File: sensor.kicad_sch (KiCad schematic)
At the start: 35 parts, among them J5 Conn_01x07_Pin, J8 Conn_01x08_Pin, U3 MIC5323-3.3YD5-TR

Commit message: Cleanup libraries
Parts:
- LED6: symbol marbastlib:SK6812MINI-E -> Marbastlib:SK6812MINI-E
- U3: symbol mcp5323:MIC5323-3.3YD5-TR -> Mcp5323:MIC5323-3.3YD5-TR
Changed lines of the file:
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@@
     )
   )
-  (symbol (lib_id "marbastlib:SK6812MINI-E") (at 204.47 91.44 0) (unit 1)
+  (symbol (lib_id "Marbastlib:SK6812MINI-E") (at 204.47 91.44 0) (unit 1)
     (in_bom yes) (on_board yes) (dnp no)
     (property "Reference" "LED6" (at 210.82 99.06 0)
@@
     )
   )
-  (symbol (lib_id "mcp5323:MIC5323-3.3YD5-TR") (at 189.23 34.29 0) (unit 1)
+  (symbol (lib_id "Mcp5323:MIC5323-3.3YD5-TR") (at 189.23 34.29 0) (unit 1)
     (in_bom yes) (on_board yes) (dnp no) (fields_autoplaced)
     (property "Reference" "U3" (at 203.2 26.67 0)

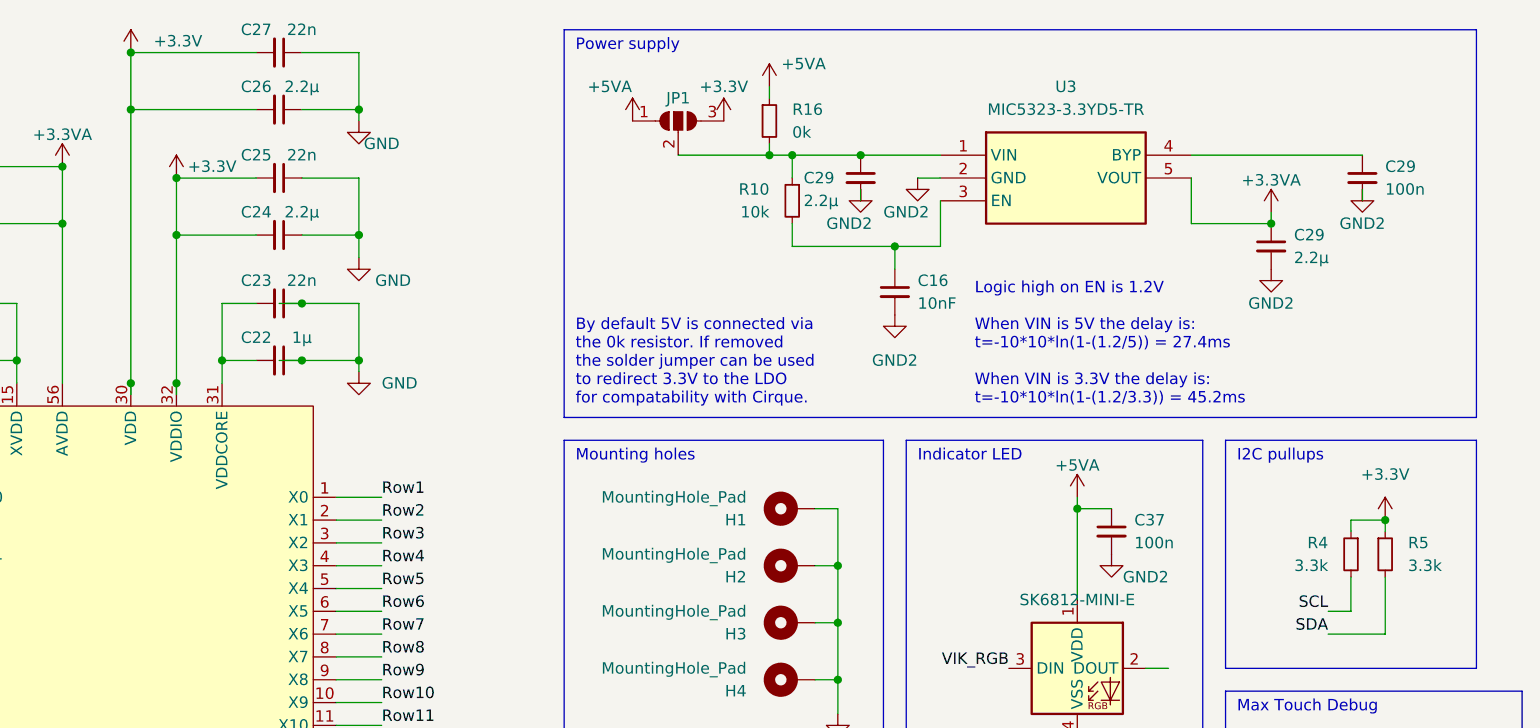
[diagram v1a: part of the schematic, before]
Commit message: Switch LDO for a cheaper part.
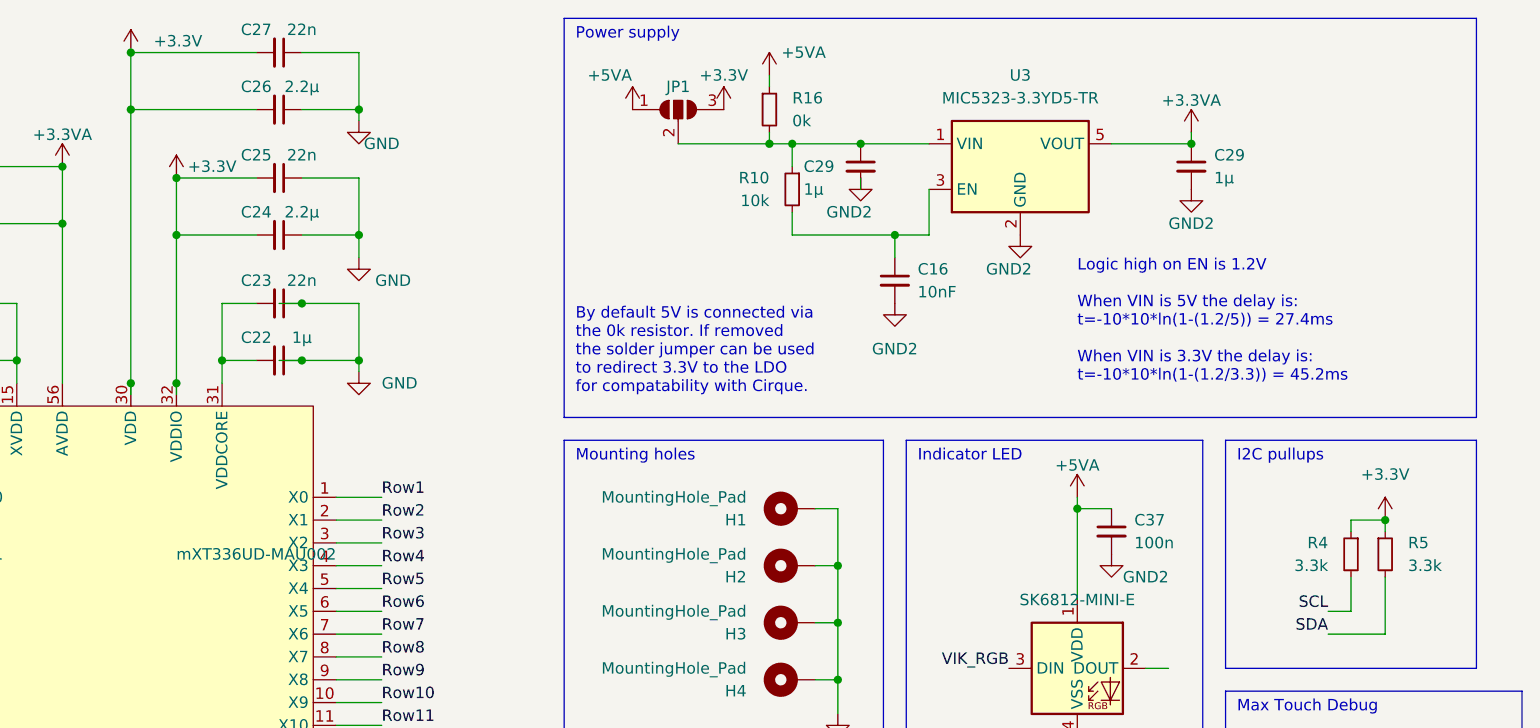
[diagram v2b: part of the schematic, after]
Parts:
- removed C29: 100n, Capacitor_SMD:C_0402_1005Metric, symbol Device:C_Small
- C29: value 2.2µ -> 1µ
- U3: footprint Trackpad:SOT95P280X100-5N -> Package_TO_SOT_SMD:SOT-23-5; symbol Mcp5323:MIC5323-3.3YD5-TR -> Regulator_Linear:MIC5504-3.3YM5; LCSC C512211 -> C88419
- mXT336UD-MAU1: value ~ -> mXT336UD-MAU002
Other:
- moved on the sheet: C16, C29, JP1, R10, R16

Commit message: Move USB port closer to the edge, Additional silkscreen, Add reset header, shrink LDO caps, swap QSPI flash.
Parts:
- C29: footprint Capacitor_SMD:C_0603_1608Metric -> Capacitor_SMD:C_0402_1005Metric
- U3: LCSC C88419 -> C512211
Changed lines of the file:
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@@
       (effects (font (size 1.27 1.27)) (justify left))
     )
-    (property "Footprint" "Capacitor_SMD:C_0603_1608Metric" (at 217.17 35.56 0)
+    (property "Footprint" "Capacitor_SMD:C_0402_1005Metric" (at 217.17 35.56 0)
       (effects (font (size 1.27 1.27)) hide)
     )
@@
       (effects (font (size 1.27 1.27)) (justify left))
     )
-    (property "Footprint" "Capacitor_SMD:C_0603_1608Metric" (at 180.34 35.56 0)
+    (property "Footprint" "Capacitor_SMD:C_0402_1005Metric" (at 180.34 35.56 0)
       (effects (font (size 1.27 1.27)) hide)
     )
@@
       (effects (font (size 1.27 1.27)) (justify left top) hide)
     )
-    (property "LCSC" "C88419" (at 212.09 27.94 0)
-      (effects (font (size 1.27 1.27)) hide)
-    )
+    (property "LCSC" "C512211" (at 212.09 27.94 0)
+      (effects (font (size 1.27 1.27)) hide)
+    )

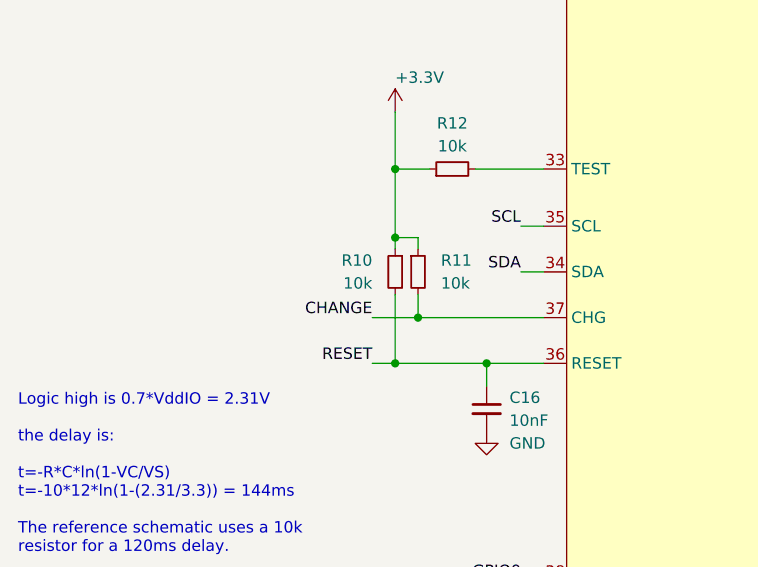
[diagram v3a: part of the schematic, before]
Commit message: Re-route to avoid crossing the USB data lines. Reduced keys to 5 to avoid having to route a long trace around the crystal, swaped key footprint from choc hotswap to mx/choc combined soldered.
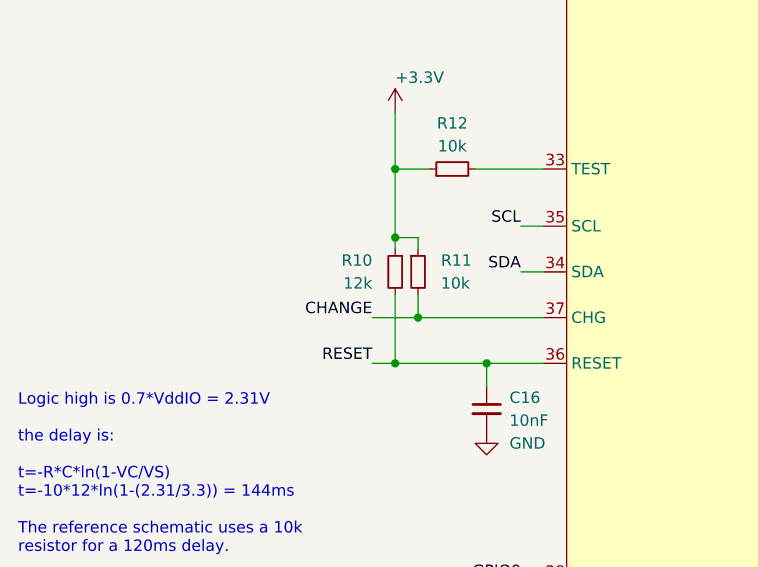
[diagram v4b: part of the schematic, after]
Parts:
- R10: value 10k -> 12k
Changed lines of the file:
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@@
       (effects (font (size 1.27 1.27)) (justify left))
     )
-    (property "Value" "10k" (at 55.88 125.73 0)
+    (property "Value" "12k" (at 55.88 125.73 0)
       (effects (font (size 1.27 1.27)) (justify left))
     )

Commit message: Minor cleanups. Made the mounting hole distances round numbers, cleaned up a few traces.
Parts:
- added J10: Conn_01x01_Pin, Connector_PinHeader_1.27mm:PinHeader_1x01_P1.27mm_Vertical, symbol Connector:Conn_01x01_Pin
- LED6: LCSC C5200774 -> C5149201
- U3: value MIC5323-3.3YD5-TR -> MIC5504-3.3YM5; LCSC C512211 -> C88419
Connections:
- net +3.3VA: now also J10.1 (Pin_1)
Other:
- note added: "AVCC 3.3V"
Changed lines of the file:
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@@
+    (stroke (width 0) (type default))
+  )
+  (wire (pts (xy 238.76 135.89) (xy 246.38 135.89))
     (stroke (width 0) (type default))
   )
@@
   (wire (pts (xy 68.58 134.62) (xy 74.93 134.62))
     (stroke (width 0) (type default))
+  )
+  (rectangle (start 220.98 125.73) (end 254 139.7)
+    (stroke (width 0) (type default))
+    (fill (type none))
   )
   (rectangle (start 147.32 19.05) (end 248.92 63.5)
@@
     (effects (font (size 1.27 1.27)) (justify left bottom))
   )
+  (text "AVCC 3.3V" (at 222.25 128.27 0)
+    (effects (font (size 1.27 1.27)) (justify left bottom))
+  )
   (text "Max Touch Debug" (at 222.25 96.52 0)
     (effects (font (size 1.27 1.27)) (justify left bottom))
@@
         (path "/3796446b-0052-4d89-b512-07a2e9135d0d/2780c9a8-e5e0-42e8-93d7-9eb6f8aa439b"
           (reference "J5") (unit 1)
+        )
+      )
+    )
+  )
+  (symbol (lib_id "Connector:Conn_01x01_Pin") (at 233.68 135.89 0) (unit 1)
+    (in_bom yes) (on_board yes) (dnp no) (fields_autoplaced)
+    (property "Reference" "J10" (at 234.315 130.81 0)
+      (effects (font (size 1.27 1.27)))
+    )
+    (property "Value" "Conn_01x01_Pin" (at 234.315 133.35 0)
+      (effects (font (size 1.27 1.27)))
+    )
+    (property "Footprint" "Connector_PinHeader_1.27mm:PinHeader_1x01_P1.27mm_Vertical" (at 233.68 135.89 0)
+      (effects (font (size 1.27 1.27)) hide)
+    )
+    (property "Datasheet" "~" (at 233.68 135.89 0)
+      (effects (font (size 1.27 1.27)) hide)
+    )
+    (pin "1")
+    (instances
+      (project "trackpad"
+        (path "/3796446b-0052-4d89-b512-07a2e9135d0d/2780c9a8-e5e0-42e8-93d7-9eb6f8aa439b"
+          (reference "J10") (unit 1)
         )
       )
@@
         (path "/3796446b-0052-4d89-b512-07a2e9135d0d/2780c9a8-e5e0-42e8-93d7-9eb6f8aa439b"
           (reference "#PWR079") (unit 1)
+        )
+      )
+    )
+  )
+  (symbol (lib_id "power:+3.3VA") (at 246.38 135.89 0) (unit 1)
+    (in_bom yes) (on_board yes) (dnp no)
+    (property "Reference" "#PWR016" (at 246.38 139.7 0)
+      (effects (font (size 1.27 1.27)) hide)
+    )
+    (property "Value" "+3.3VA" (at 246.38 132.334 0)
+      (effects (font (size 1.27 1.27)))
+    )
+    (property "Footprint" "" (at 246.38 135.89 0)
+      (effects (font (size 1.27 1.27)) hide)
+    )
+    (property "Datasheet" "" (at 246.38 135.89 0)
+      (effects (font (size 1.27 1.27)) hide)
+    )
+    (pin "1")
+    (instances
+      (project "trackpad"
+        (path "/3796446b-0052-4d89-b512-07a2e9135d0d"
+          (reference "#PWR016") (unit 1)
+        )
+        (path "/3796446b-0052-4d89-b512-07a2e9135d0d/efc97fde-28db-4fd6-89b1-84dafa779b4e"
+          (reference "#PWR048") (unit 1)
+        )
+        (path "/3796446b-0052-4d89-b512-07a2e9135d0d/2780c9a8-e5e0-42e8-93d7-9eb6f8aa439b"
+          (reference "#PWR066") (unit 1)
         )
       )
@@
       (effects (font (size 1.27 1.27)) hide)
     )
-    (property "LCSC" "C5200774" (at 210.82 99.06 0)
+    (property "LCSC" "C5149201" (at 210.82 99.06 0)
       (effects (font (size 1.27 1.27)) hide)
     )
@@
         )
         (path "/3796446b-0052-4d89-b512-07a2e9135d0d/2780c9a8-e5e0-42e8-93d7-9eb6f8aa439b"
-          (reference "LED7") (unit 1)
+          (reference "LED6") (unit 1)
         )
       )
@@
       (effects (font (size 1.27 1.27)))
     )
-    (property "Value" "MIC5323-3.3YD5-TR" (at 198.12 27.94 0)
+    (property "Value" "MIC5504-3.3YM5" (at 198.12 27.94 0)
       (effects (font (size 1.27 1.27)))
     )
@@
       (effects (font (size 1.27 1.27)) (justify left top) hide)
     )
-    (property "LCSC" "C512211" (at 212.09 27.94 0)
-      (effects (font (size 1.27 1.27)) hide)
-    )
+    (property "LCSC" "C88419" (at 212.09 27.94 0)
+      (effects (font (size 1.27 1.27)) hide)
+    )

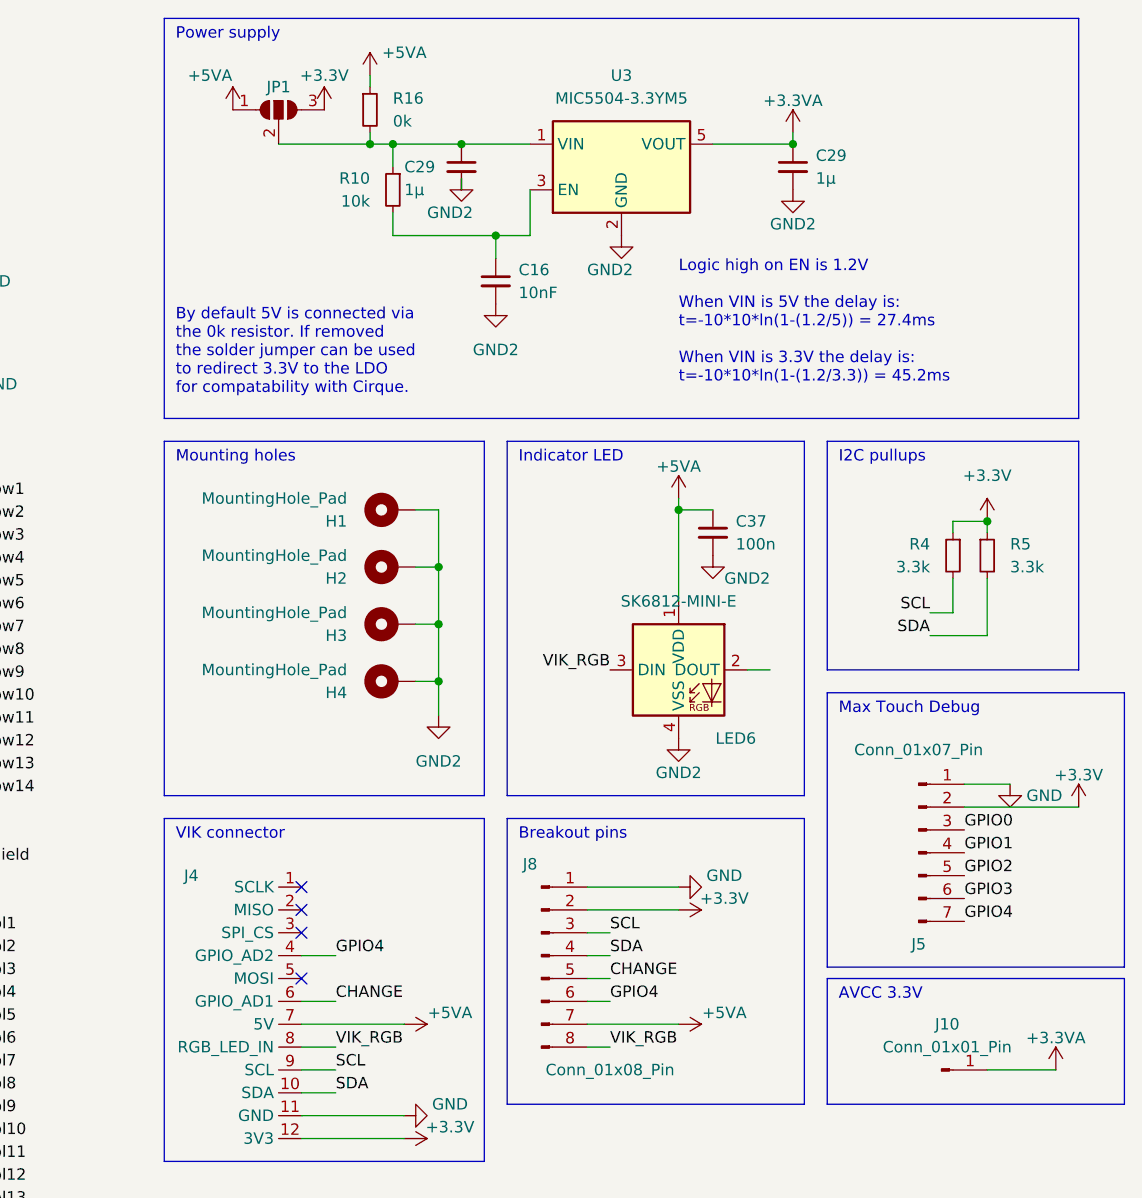
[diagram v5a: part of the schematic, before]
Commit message: Modify EC11 footprint to allow SMT parts. Add resistors to the LED data lines.
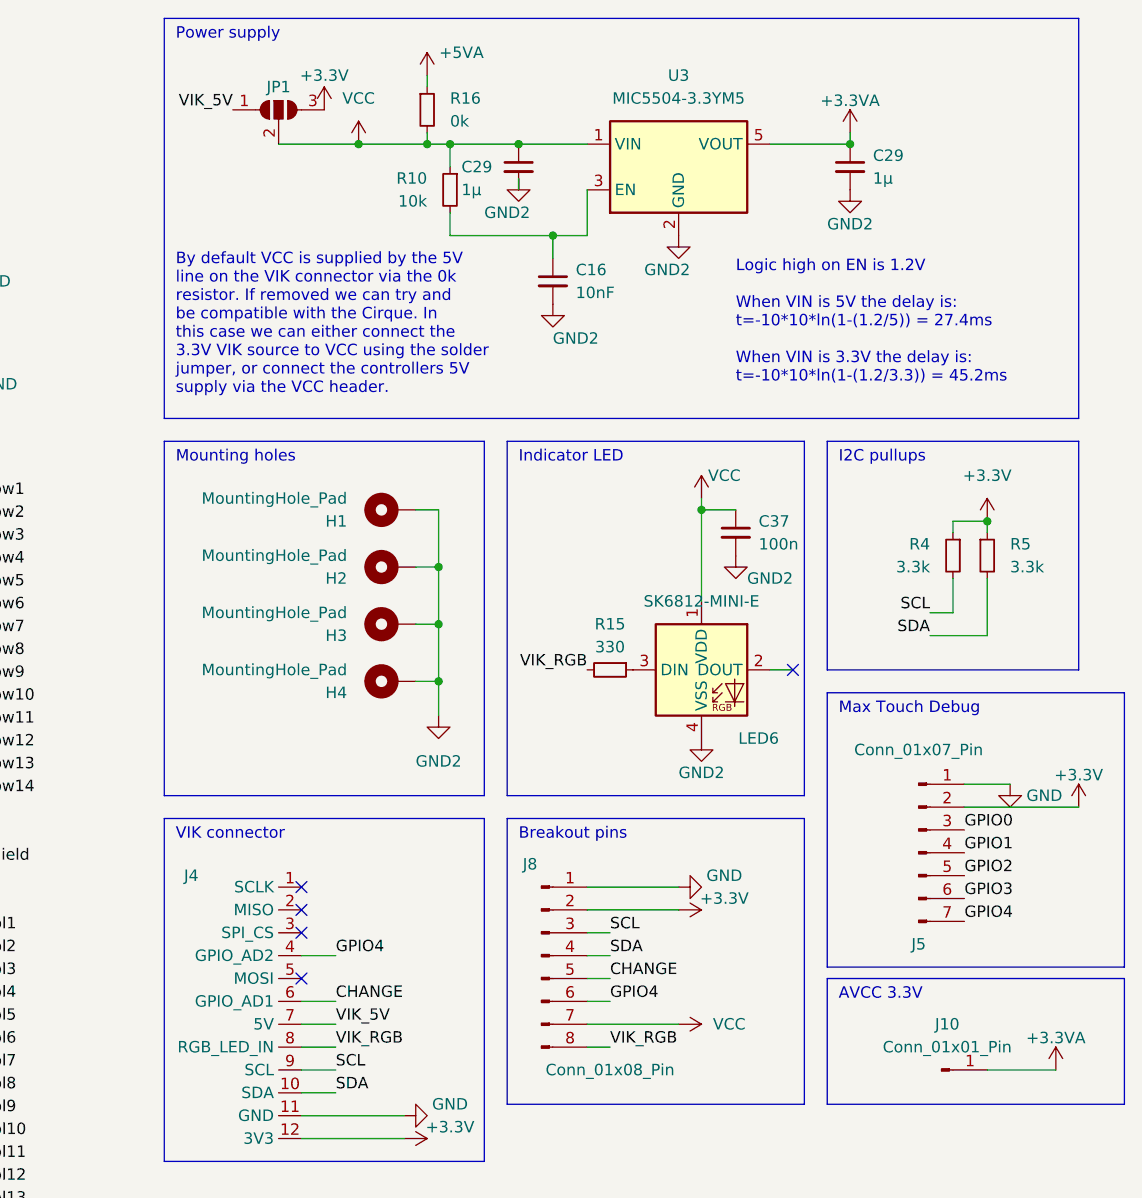
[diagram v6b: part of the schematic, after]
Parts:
- added R15: 330, Resistor_SMD:R_0402_1005Metric, symbol Device:R_Small
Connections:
- net +5VA: no longer C37.1, J4.7 (5V), J8.7 (Pin_7), JP1.1 (A), LED6.1 (VDD)
- net VIK_RGB: now also R15.2; no longer LED6.3 (DIN)
- net VCC: now reaches C29.1, JP1.2 (C), R10.1, R16.2, U3.1 (VIN)
- net VCC: now also C37.1, J8.7 (Pin_7), LED6.1 (VDD)
- new net: LED6.3 (DIN), R15.1
- new net VIK_5V: J4.7 (5V), JP1.1 (A)
- no-connect marks 4 -> 5
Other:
- note added: "By default VCC is supplied by the 5V line on the VIK connector via the 0k resistor. If removed we can try and be compatible with the Cirque. In this case we can either connect the 3.3V VIK source to VCC using the solder jumper, or connect the controllers 5V supply via the VCC header."
- note removed: "By default 5V is connected via the 0k resistor. If removed the solder jumper can be used to redirect 3.3V to the LDO for compatability with Cirque."
- moved on the sheet: C16, C29, C37, LED6, R10, R16, U3

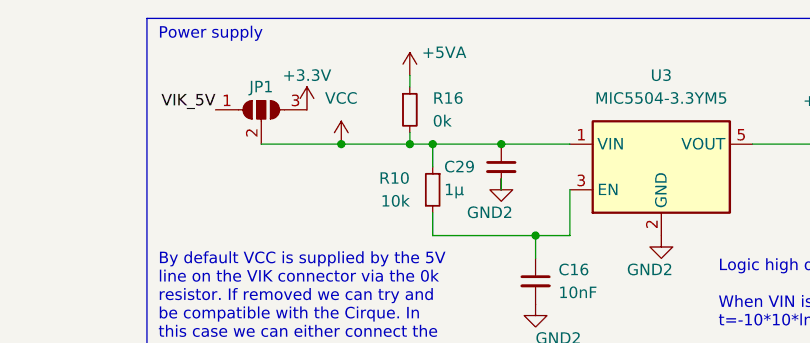
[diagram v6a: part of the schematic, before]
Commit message: Fix DRC issue and add VCC warning.
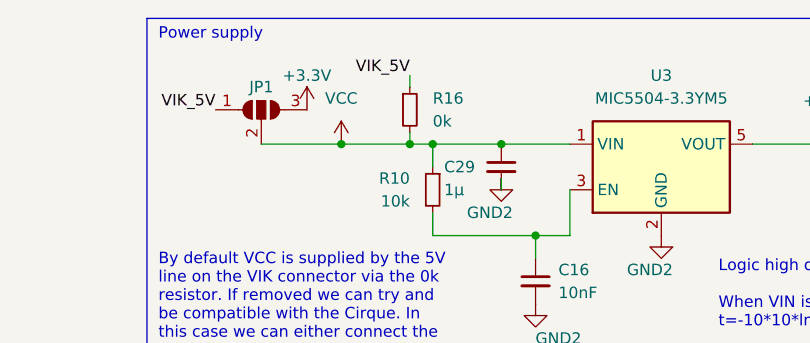
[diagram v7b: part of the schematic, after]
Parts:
- R15: LCSC C25104 -> (none)
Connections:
- net +5VA is gone; now on net VIK_5V: R16.1
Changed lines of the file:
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@@
     (effects (font (size 1.27 1.27)) (justify left bottom))
+  )
+  (label "VIK_5V" (at 176.53 25.4 180) (fields_autoplaced)
+    (effects (font (size 1.27 1.27)) (justify right bottom))
   )
   (label "SCL" (at 72.39 119.38 180) (fields_autoplaced)
@@
     )
   )
-  (symbol (lib_id "power:+5VA") (at 176.53 25.4 0) (unit 1)
-    (in_bom yes) (on_board yes) (dnp no)
-    (property "Reference" "#PWR015" (at 176.53 29.21 0)
-      (effects (font (size 1.27 1.27)) hide)
-    )
-    (property "Value" "+5VA" (at 180.34 22.86 0)
-      (effects (font (size 1.27 1.27)))
-    )
-    (property "Footprint" "" (at 176.53 25.4 0)
-      (effects (font (size 1.27 1.27)) hide)
-    )
-    (property "Datasheet" "" (at 176.53 25.4 0)
-      (effects (font (size 1.27 1.27)) hide)
-    )
-    (pin "1")
-    (instances
-      (project "trackpad"
-        (path "/3796446b-0052-4d89-b512-07a2e9135d0d"
-          (reference "#PWR015") (unit 1)
-        )
-        (path "/3796446b-0052-4d89-b512-07a2e9135d0d/efc97fde-28db-4fd6-89b1-84dafa779b4e"
-          (reference "#PWR047") (unit 1)
-        )
-        (path "/3796446b-0052-4d89-b512-07a2e9135d0d/2780c9a8-e5e0-42e8-93d7-9eb6f8aa439b"
-          (reference "#PWR0104") (unit 1)
-        )
-      )
-    )
-  )
   (symbol (lib_id "power:GND2") (at 210.82 78.74 0) (unit 1)
     (in_bom yes) (on_board yes) (dnp no)
@@
       (effects (font (size 1.27 1.27)) hide)
     )
-    (property "LCSC" "C25104" (at 196.85 86.36 0)
-      (effects (font (size 1.27 1.27)) hide)
-    )
